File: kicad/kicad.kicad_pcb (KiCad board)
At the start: 2 copper layers, 100 x 100 mm, 105 parts, among them J101 DEBUG_LED_CONN, J102 EPD_SPI_CONN, J103 HPC_CONN, J104 STORAGE_CONN, J105 USBC_CONN, J106 GLOBAL_CONN, J107 INPUT_CONN, J201 USB_C_Receptacle_USB2.0_16P, J301 BATTERY_CONN, J501 MOTOR_P_SF, J502 MOTOR_N_SF, Q401 SI1308EDL, SW1 PLACEHOLDER_BT1, SW2 PLACEHOLDER_BT2, SW3 PLACEHOLDER_BT3, SW301 SW_Push, SW701 BT1, SW702 BT2, SW703 BT3, SW704 BT4, U201 TPD2S300, U301 BQ21061, U501 DA7280, U601 M95P32

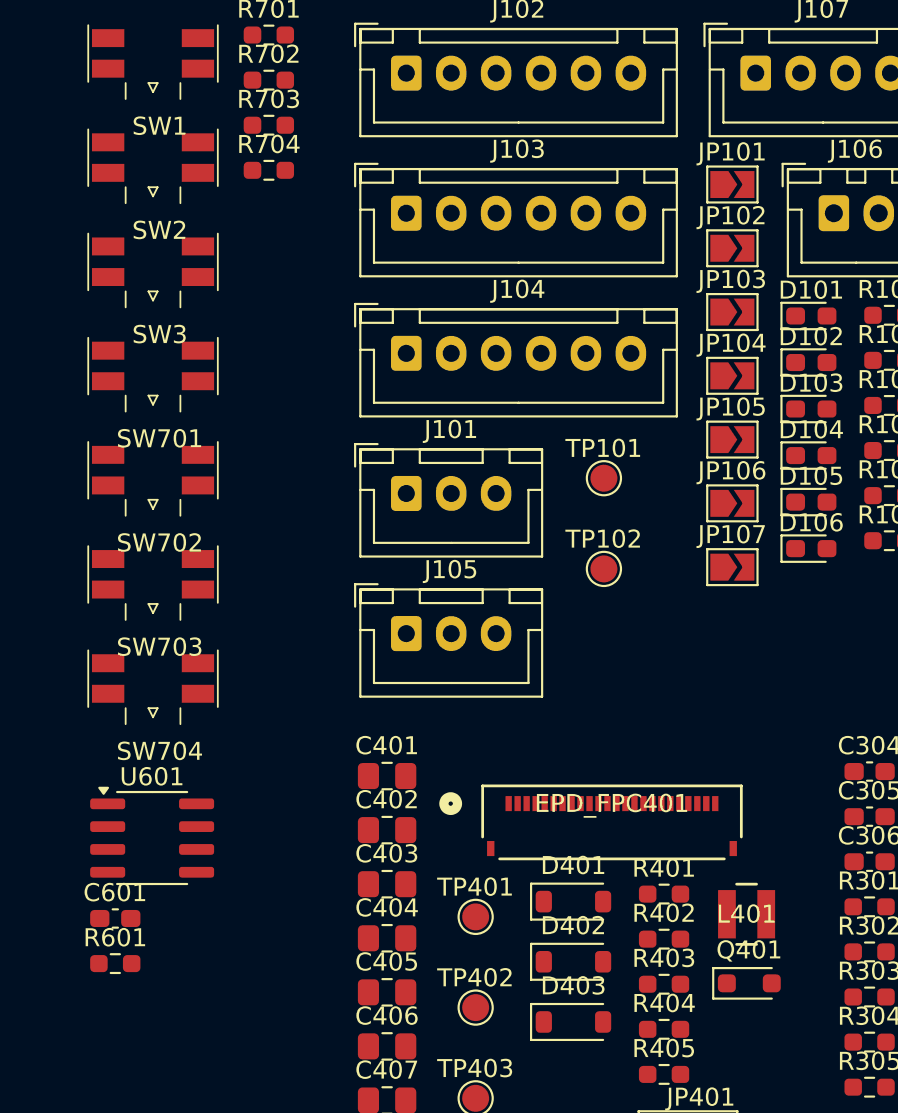
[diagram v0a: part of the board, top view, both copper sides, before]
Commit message: fix errors/update USB-c footprint, DA7280 footprint still needs fixing
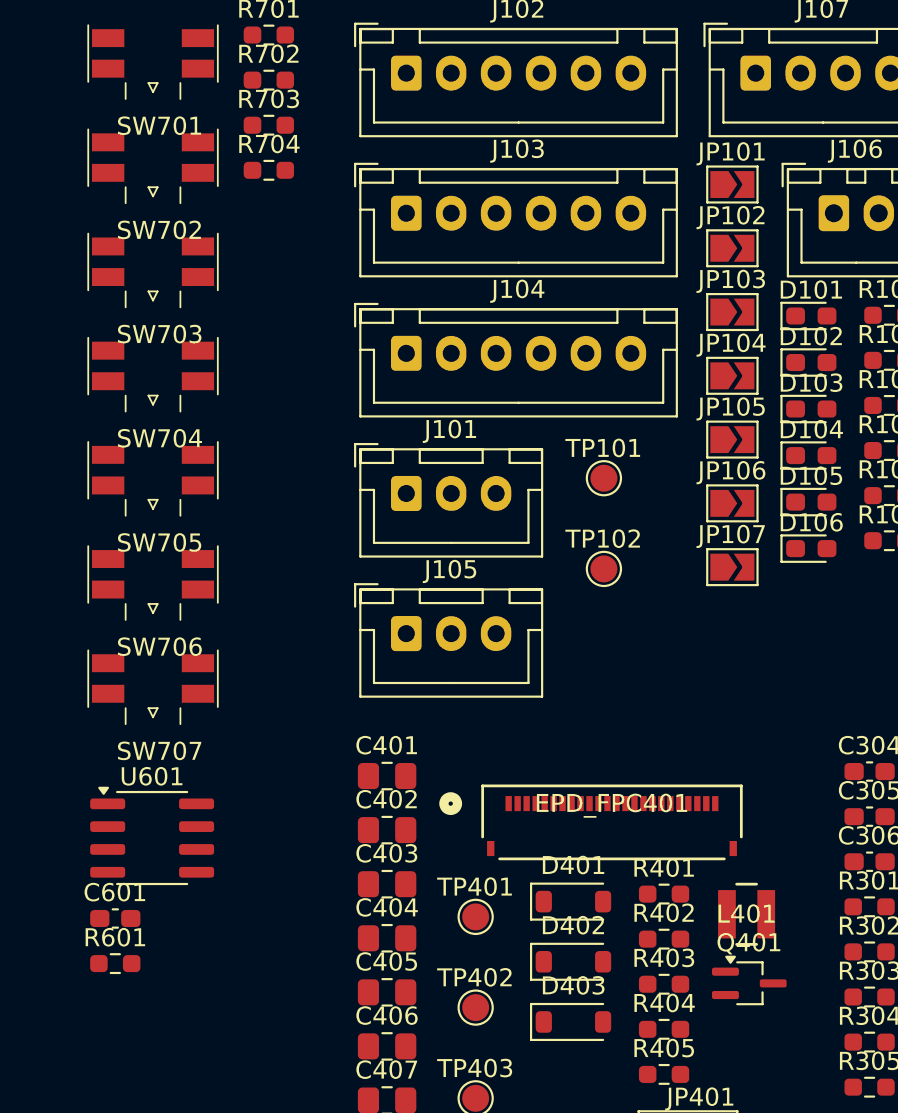
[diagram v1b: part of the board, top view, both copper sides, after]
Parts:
- Q401: footprint Diode_SMD:D_SOD-323_HandSoldering -> Package_TO_SOT_SMD:SOT-323_SC-70_Handsoldering
- U501: footprint Package_DFN_QFN:QFN-12-1EP_3x3mm_P0.5mm_EP1.65x1.65mm -> Raven:QFN-12_3x3mm_P0.65mm
- renumbered SW1 to SW701, SW2 to SW702, SW3 to SW703, SW701 to SW704, SW702 to SW705, SW703 to SW706, SW704 to SW707
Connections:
- EPD_FPC401 pad 25: (no net) -> unconnected-(EPD_FPC401-MNT_NC-Pad25)
- EPD_FPC401 pad 26: (no net) -> unconnected-(EPD_FPC401-MNT_NC-Pad26)
- U501 pad 13: (no net) -> unconnected-(U501-IC_NC-Pad13)

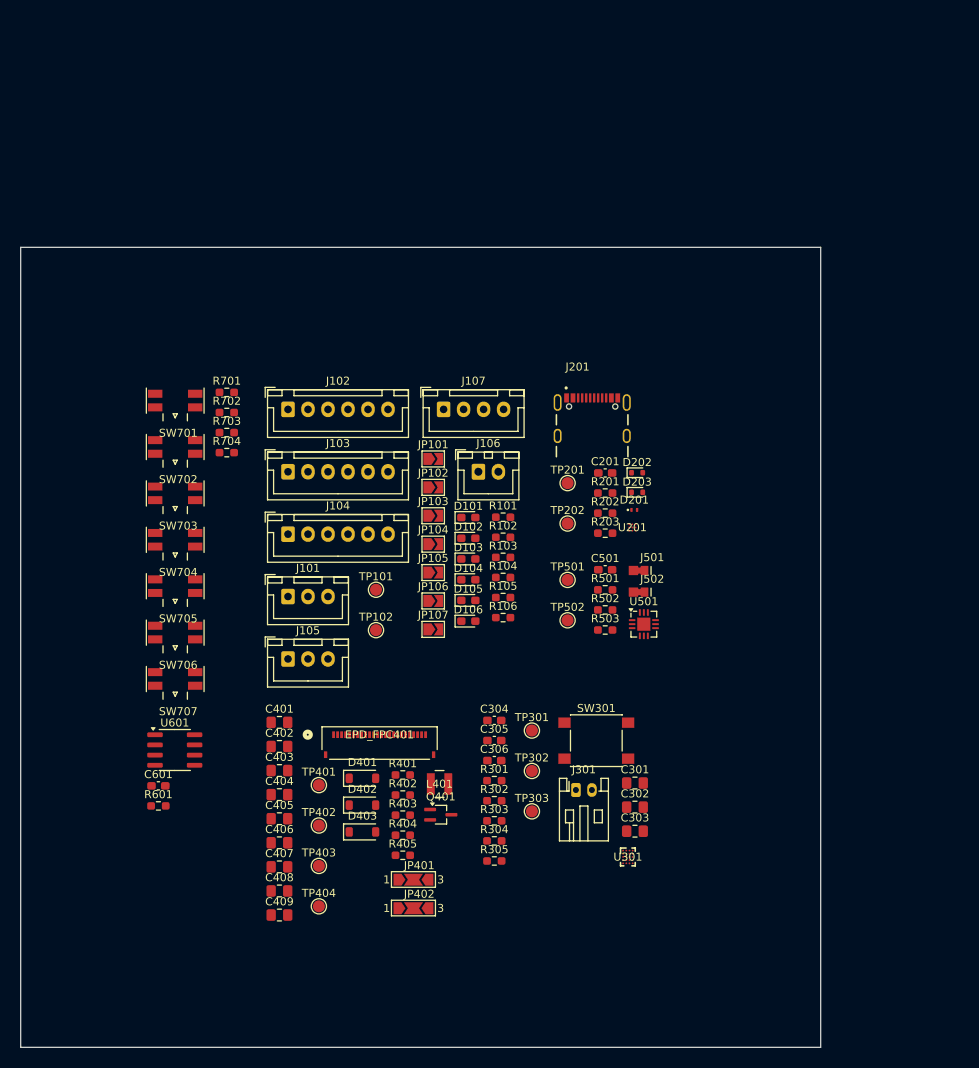
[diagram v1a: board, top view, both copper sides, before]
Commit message: PCB almost finished: only battery & usb-c needed
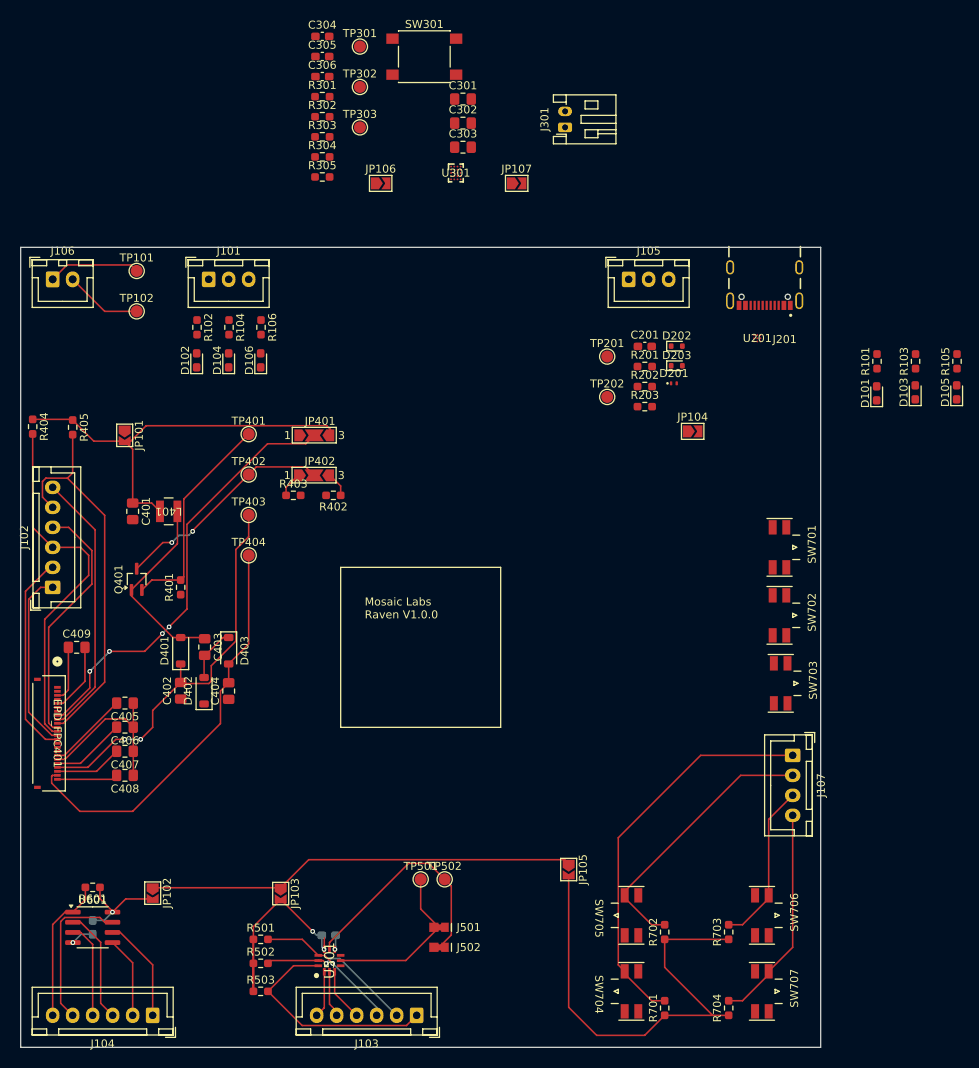
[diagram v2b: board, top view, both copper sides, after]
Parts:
- C501, C601: moved to B.Cu
- U501: footprint Raven:QFN-12_3x3mm_P0.65mm -> Raven:QFN-12-3x3mm-P0.65mm
- moved R701 94.4 mm to (173.5, 142.1), turned to 90 degrees
- moved R704 93.6 mm to (181.5, 142.1), turned to 90 degrees
- moved R703 88.5 mm to (181.5, 132.6), turned to 90 degrees
- moved C301 88.2 mm to (148.3, 28.5)
- moved C302 88.2 mm to (148.3, 31.5)
- moved C303 88.2 mm to (148.3, 34.5)
- moved C304 88.2 mm to (130.7, 20.6)
- moved C305 88.2 mm to (130.7, 23.1)
- moved C306 88.2 mm to (130.7, 25.7)
- moved R301 88.2 mm to (130.7, 28.2)
- moved R302 88.2 mm to (130.7, 30.7)
- moved R303 88.2 mm to (130.7, 33.2)
- moved R304 88.2 mm to (130.7, 35.7)
- moved R305 88.2 mm to (130.7, 38.2)
- moved SW301 88.2 mm to (143.5, 23.2)
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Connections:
- EPD_FPC401 pad 3: GND -> /E-Paper Display/RESE
- J102 pad 3: /CS -> /E-Paper Display/CS_N
- J102 pad 5: /RES -> /E-Paper Display/RES_N
- JP402 pad 2: GND -> /E-Paper Display/RESE
- Q401 pad 3: GND -> /E-Paper Display/RESE
- TP402 pad 1: GND -> /E-Paper Display/RESE
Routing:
- net +3.3V: track 0.00 -> 65.2 mm
- net /Input/PULL_UP: track 0.00 -> 59.0 mm
- net /E-Paper Display/BS: track 0.00 -> 54.1 mm, vias 0 -> 4
- net /E-Paper Display/PWR: track 0.00 -> 52.1 mm
- net /E-Paper Display/PREVGL: track 0.00 -> 51.2 mm
- net /E-Paper Display/PREVGH: track 0.00 -> 50.1 mm, vias 0 -> 2
- net /Input/BT1: track 0.00 -> 49.8 mm
- net /E-Paper Display/RES_N: track 0.00 -> 48.2 mm
- net /E-Paper Display/CS_N: track 0.00 -> 45.4 mm
- net GND: track 0.00 -> 42.4 mm, vias 0 -> 2
- net /Input/BT2: track 0.00 -> 34.2 mm
- net /E-Paper Display/BUSY: track 0.00 -> 33.6 mm
- net /Haptics/PWR: track 0.00 -> 33.3 mm, vias 0 -> 2
- net /E-Paper Display/DC: track 0.00 -> 31.2 mm
- net /Haptics/OUTN_T: track 0.00 -> 29.7 mm
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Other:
- board text added: "Mosaic Labs Raven V1.0.0"

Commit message: finish PCB routing, need silkscreen + checks
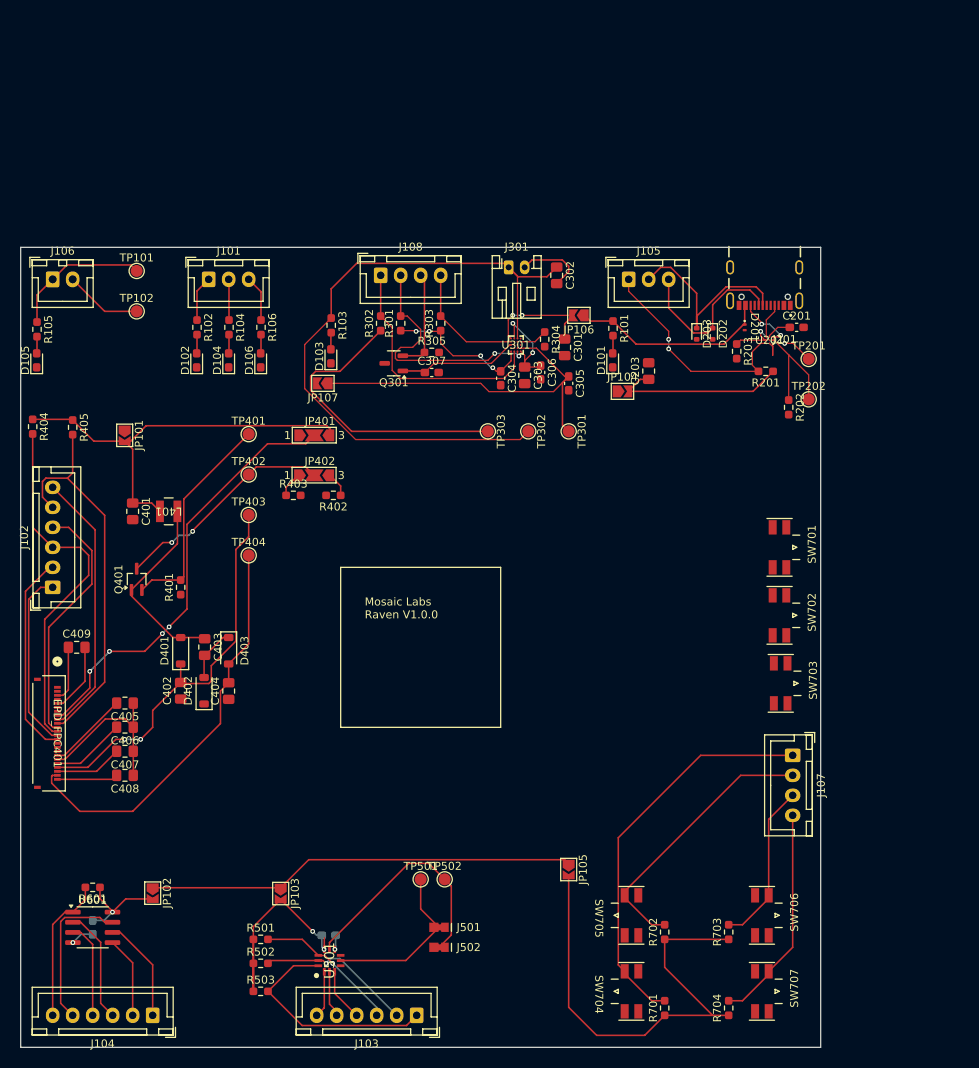
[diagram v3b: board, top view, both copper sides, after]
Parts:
- removed SW301: SW_Push, Button_Switch_SMD:SW_Push_1P1T_NO_6x6mm_H9.5mm
- added C203: 1uF, Capacitor_SMD:C_0805_2012Metric_Pad1.18x1.45mm_HandSolder, F.Cu at (171.5, 62.5)
- added C307: 100nF, Capacitor_SMD:C_0603_1608Metric_Pad1.08x0.95mm_HandSolder, F.Cu at (144.4, 62.6)
- added J108: CHARGER_CONN, Connector_JST:JST_XH_B4B-XH-A_1x04_P2.50mm_Vertical, F.Cu at (138.0, 50.5)
- added Q301: 2N7002, Package_TO_SOT_SMD:SOT-23-3, F.Cu at (139.6, 61.5)
- R305: value 10k -> 100k
- moved D105 115.1 mm to (95.0, 61.1)
- moved R105 115.1 mm to (95.0, 57.2), turned to -90 degrees
- moved R103 73.2 mm to (131.8, 56.8), turned to -90 degrees
- moved D103 73.2 mm to (131.8, 60.6)
- moved TP301 54.7 mm to (161.5, 70.0), turned to -90 degrees
- moved C305 51.2 mm to (161.5, 64.0), turned to -90 degrees
- moved C304 48.2 mm to (153.0, 63.4), turned to -90 degrees
- moved TP302 47.9 mm to (156.4, 70.0), turned to -90 degrees
- moved C306 46.0 mm to (158.0, 62.6), turned to -90 degrees
- moved TP303 41.2 mm to (151.4, 70.0), turned to -90 degrees
- moved R304 36.0 mm to (158.5, 58.5), turned to -90 degrees
- moved JP107 34.8 mm to (130.8, 64.0), turned to 180 degrees
- moved C301 33.5 mm to (161.0, 59.5), turned to -90 degrees
- moved D101 33.3 mm to (167.0, 61.1)
- moved R101 33.3 mm to (167.0, 57.1), turned to -90 degrees
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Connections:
- JP106 pad 1: /Battery Management V2/CHRG -> VBUS
- JP106 pad 2: VBUS -> /Battery Management V2/CHRG
- R305 pad 1: /Battery Management V2/VIO -> /Battery Management V2/MR_CTRL
- R305 pad 2: /Battery Management V2/INT_N -> GND
- U301 pad 10: /Battery Management V2/CE_N -> unconnected-(U301-~{CE}-Pad10)
- U301 pad 14: /Battery Management V2/INT_N -> unconnected-(U301-~{INT}-Pad14)
- U301 pad 15: /Battery Management V2/LP_N -> unconnected-(U301-~{LP}-Pad15)
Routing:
- net +BATT: track 0.00 -> 84.9 mm
- net /Battery Management V2/VIO: track 0.00 -> 55.9 mm, vias 0 -> 4
- net /Battery Management V2/REG: track 0.00 -> 46.2 mm
- net /Battery Management V2/SCL: track 0.00 -> 30.8 mm, vias 0 -> 2
- net /Battery Management V2/SDA: track 0.00 -> 30.8 mm
- net /USB-C/FLT_N: track 0.00 -> 28.1 mm, vias 0 -> 2
- net /USB-C/IC_PWR: track 0.00 -> 25.5 mm
- net /USB-C/DM: track 0.00 -> 25.4 mm
- net VBUS: track 0.00 -> 24.9 mm
- net /USB-C/DP: track 0.00 -> 21.3 mm
- net /Battery Management V2/PG_N: track 0.00 -> 15.2 mm
- net Net-(Q301-D): track 0.00 -> 15.0 mm
- net /USB-C/CC2_T: track 0.00 -> 15.0 mm
- net /Battery Management V2/CHRG: track 0.00 -> 14.2 mm, vias 0 -> 2
- net Net-(U301-VINLS): track 0.00 -> 13.1 mm, vias 0 -> 2
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
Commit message: fix and place silkscreen
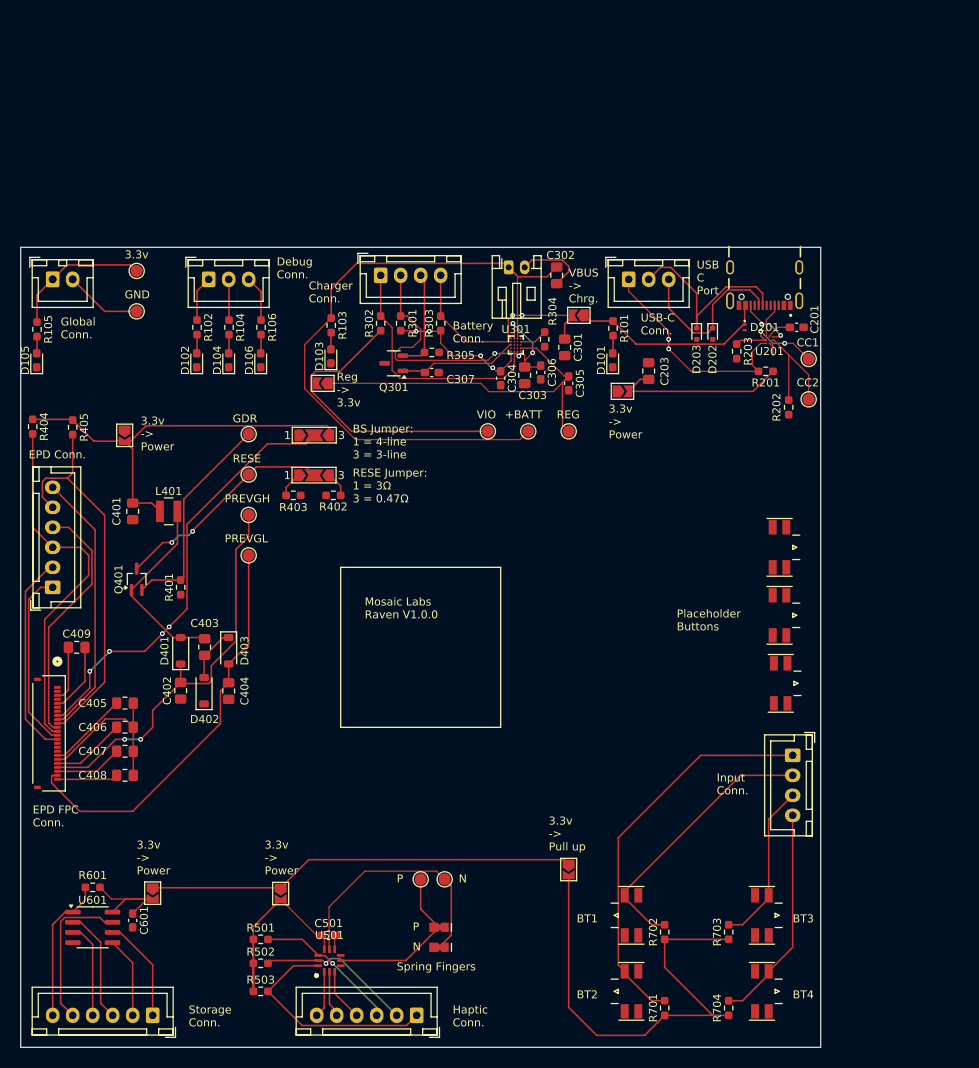
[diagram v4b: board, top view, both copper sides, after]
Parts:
- C501, C601: moved to F.Cu
- moved C601 5.07 mm to (107.0, 131.1)
- renumbered TP101 to 3.3v, TP102 to GND, TP502 to OUTN_TP, TP501 to OUTP_TP
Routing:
- net /Storage/PWR: track 12.4 -> 16.2 mm, vias 1 -> 0
- net GND: track 51.4 -> 48.5 mm, vias 2 -> 0
- net /Haptics/OUTN_T: track 29.7 -> 31.5 mm
- net /Haptics/PWR: track 33.3 -> 31.8 mm, vias 2 -> 0
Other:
- board text added: "+BATT"
- board text added: "3.3v"
- board text added: "3.3v -> Power"
- board text added: "3.3v -> Pull up"
- board text added: "BS Jumper: 1 = 4-line 3 = 3-line"
- board text added: "BT1"
- board text added: "BT2"
- board text added: "BT3"
- board text added: "BT4"
- board text added: "Battery Conn."
- board text added: "CC1"
- board text added: "CC2"
- board text added: "Charger Conn."
- board text added: "Debug Conn."
- board text added: "EPD Conn."
- board text added: "EPD FPC Conn."
- board text added: "GDR"
- board text added: "GND"
- board text added: "Global Conn."
- board text added: "Haptic Conn."
- board text added: "Input Conn."
- board text added: "N"
- board text added: "P"
- board text added: "PREVGH"
- board text added: "PREVGL"
- board text added: "Placeholder Buttons"
- board text added: "REG"
- board text added: "RESE"
- board text added: "RESE Jumper: 1 = 3Ω 3 = 0.47Ω"
- board text added: "Reg -> 3.3v"
- board text added: "Spring Fingers"
- board text added: "Storage Conn."
- board text added: "USB C Port"
- board text added: "USB-C Conn."
- board text added: "VBUS -> Chrg."
- board text added: "VIO"

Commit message: silkscreen art!
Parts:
- added G***: LOGO, LOGO, F.Cu at (150.4, 106.6)
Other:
- board text removed: "Mosaic Labs Raven V1.0.0"
